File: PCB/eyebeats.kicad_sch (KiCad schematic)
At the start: 30 parts, among them SW1 1825910-6, SW2 1825910-6, U1 MAX30102EFD_T, U2 XIAO-RP2040-DIP, U3 PCF8574T, U4 AMS1117-1.8

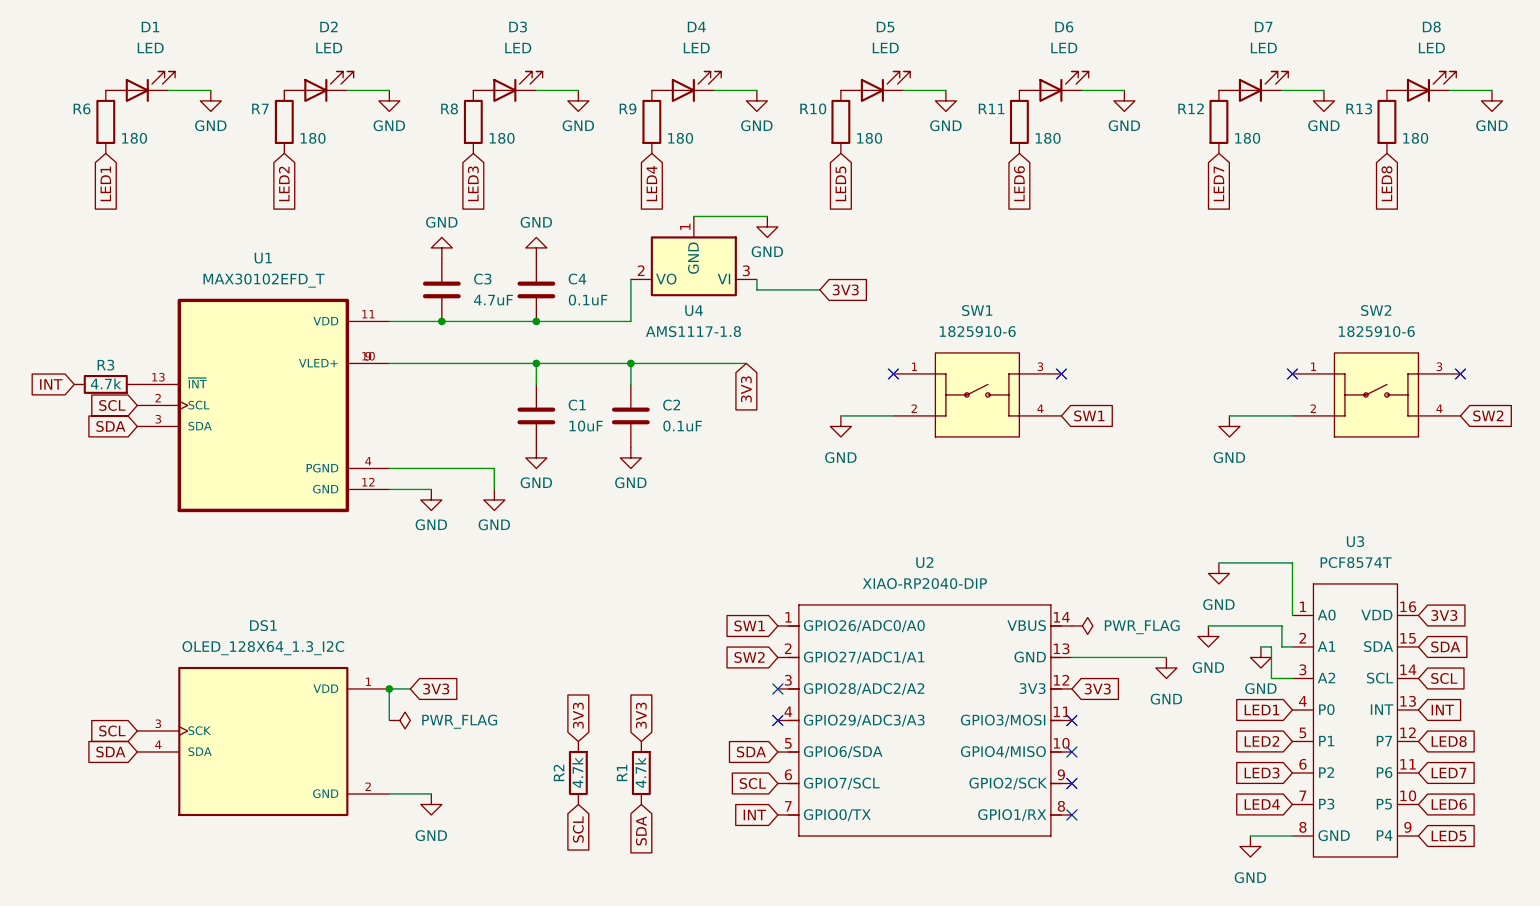
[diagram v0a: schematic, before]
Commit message: edited led directions in pcb and more codeee
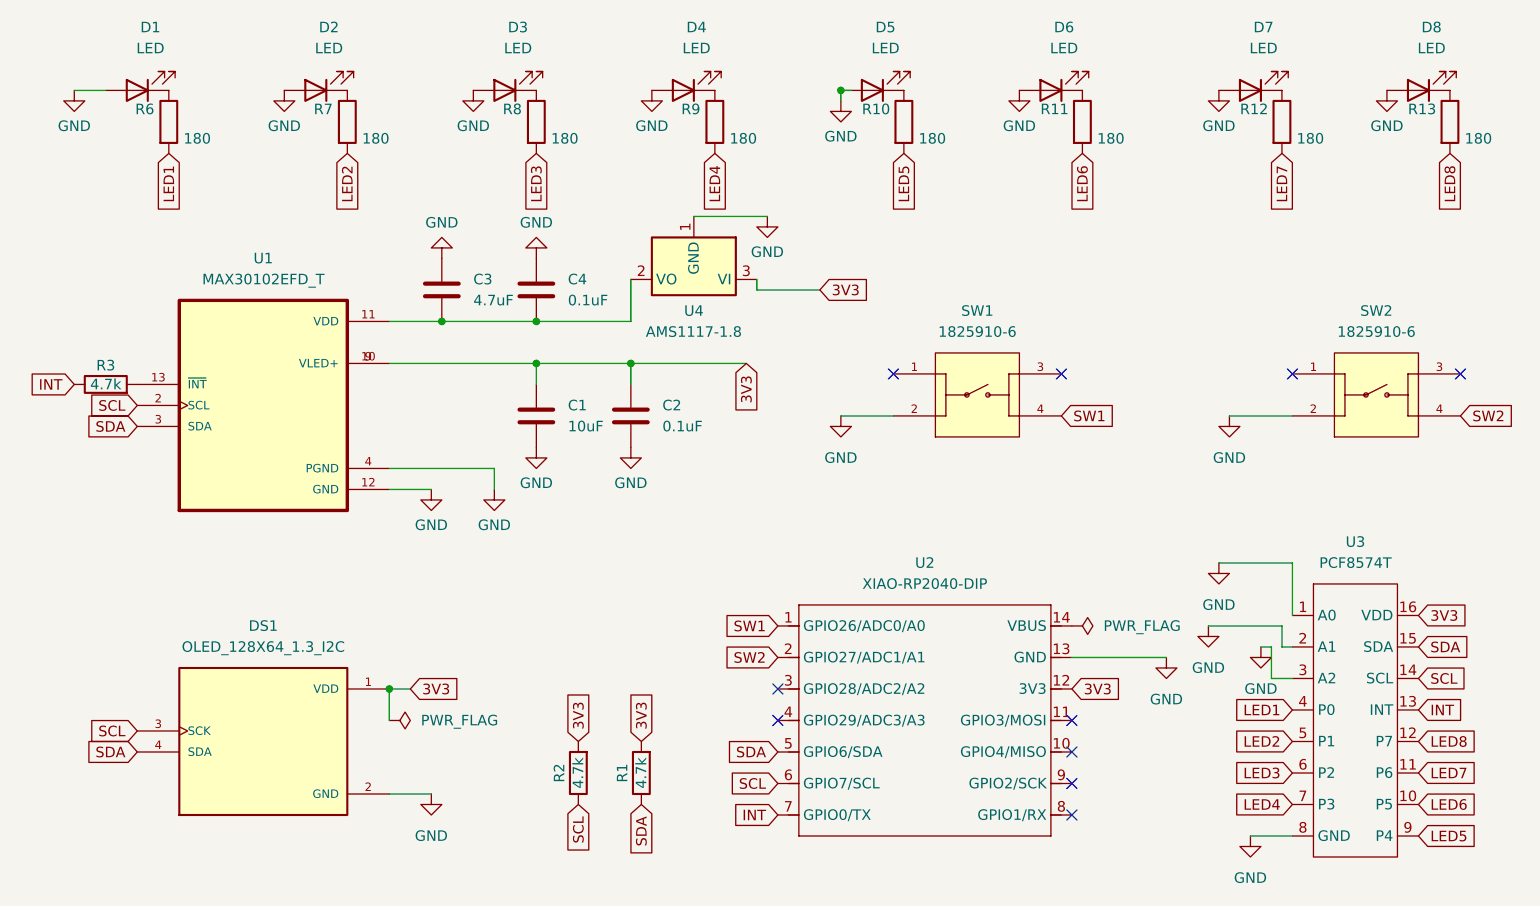
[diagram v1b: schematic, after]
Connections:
- net GND: now also D1.2 (A), D2.2 (A), D3.2 (A), D4.2 (A), D5.2 (A), D6.2 (A), D7.2 (A), D8.2 (A); no longer D1.1 (K), D2.1 (K), D3.1 (K), D4.1 (K), D5.1 (K), D6.1 (K), D7.1 (K), D8.1 (K)
- net at R7.1: now also D2.1 (K); no longer D2.2 (A)
- net at R8.1: now also D3.1 (K); no longer D3.2 (A)
- net at R6.1: now also D1.1 (K); no longer D1.2 (A)
- net at R12.1: now also D7.1 (K); no longer D7.2 (A)
- net at R11.1: now also D6.1 (K); no longer D6.2 (A)
- net at R10.1: now also D5.1 (K); no longer D5.2 (A)
- net at R13.1: now also D8.1 (K); no longer D8.2 (A)
- net at R9.1: now also D4.1 (K); no longer D4.2 (A)
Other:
- moved on the sheet: R10, R11, R12, R13, R6, R7, R8, R9
